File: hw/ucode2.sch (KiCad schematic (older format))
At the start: 16 parts, among them U801 74HC00, U802 74HC590, U803 27C64, U804 27C64, U805 27C64, U806 27C64, U807 74HCT175, U808 74HCT175, U809 74HCT175, U810 74HCT175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

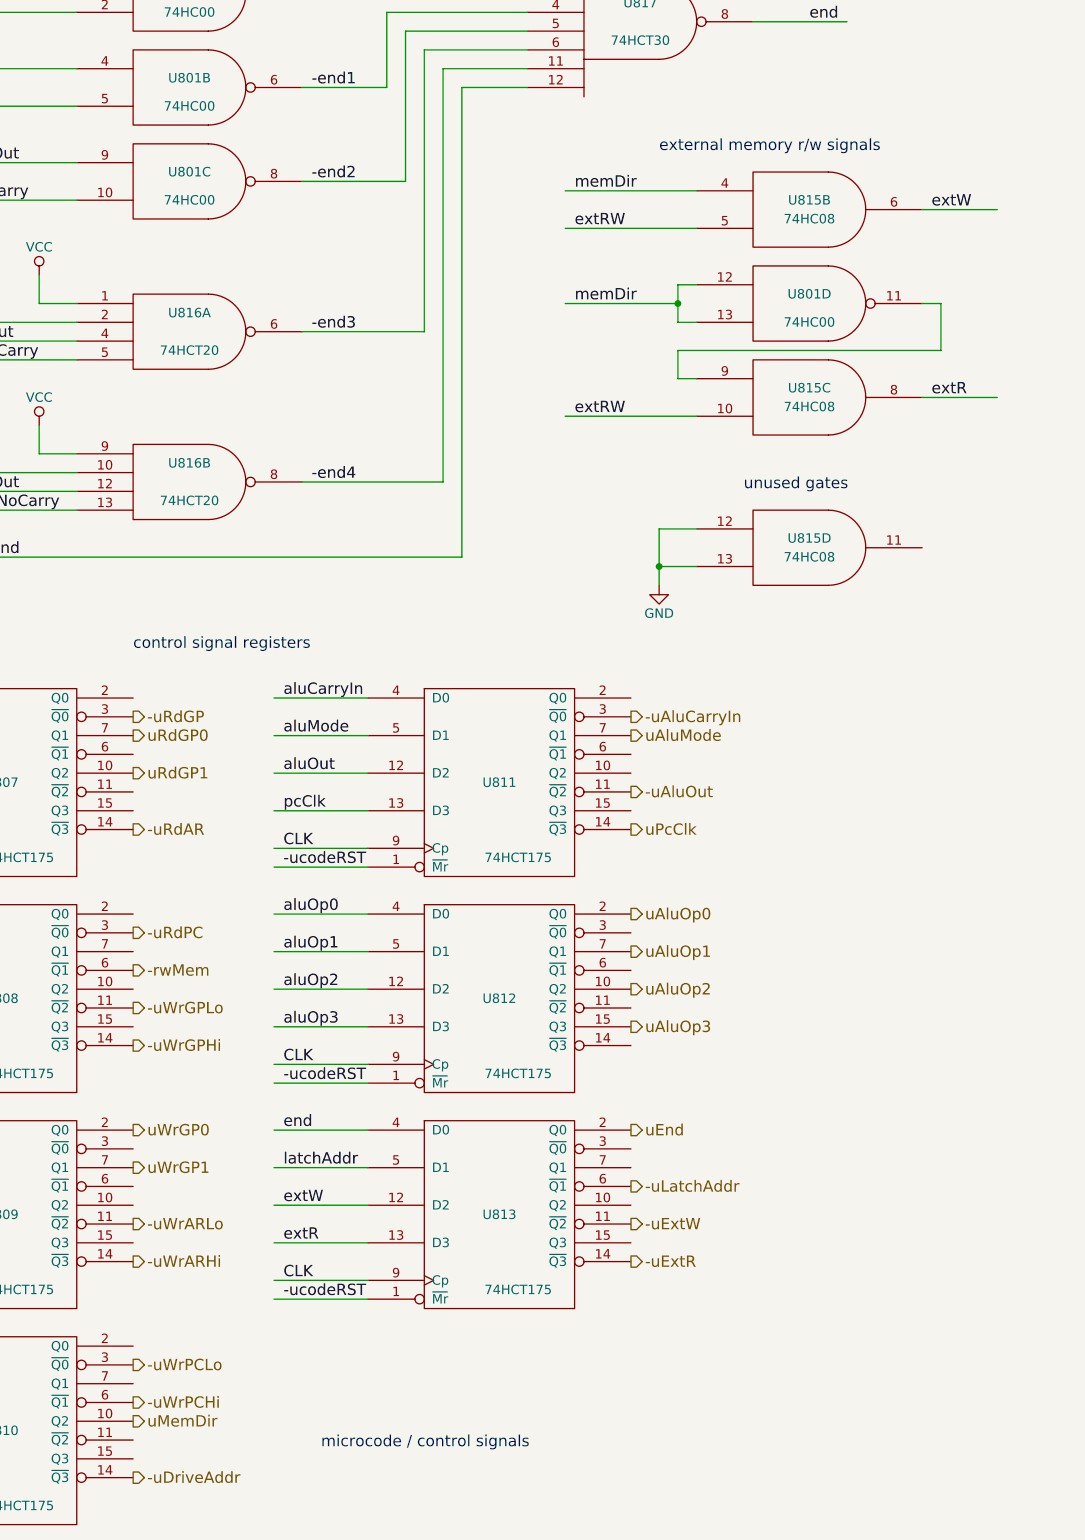
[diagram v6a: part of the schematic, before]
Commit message: do combinational logic for ext r/w after FFs
This should work fine, and allows for one more microcode
signal for latching the ALU condition codes, which I'm
pretty sure we will need.
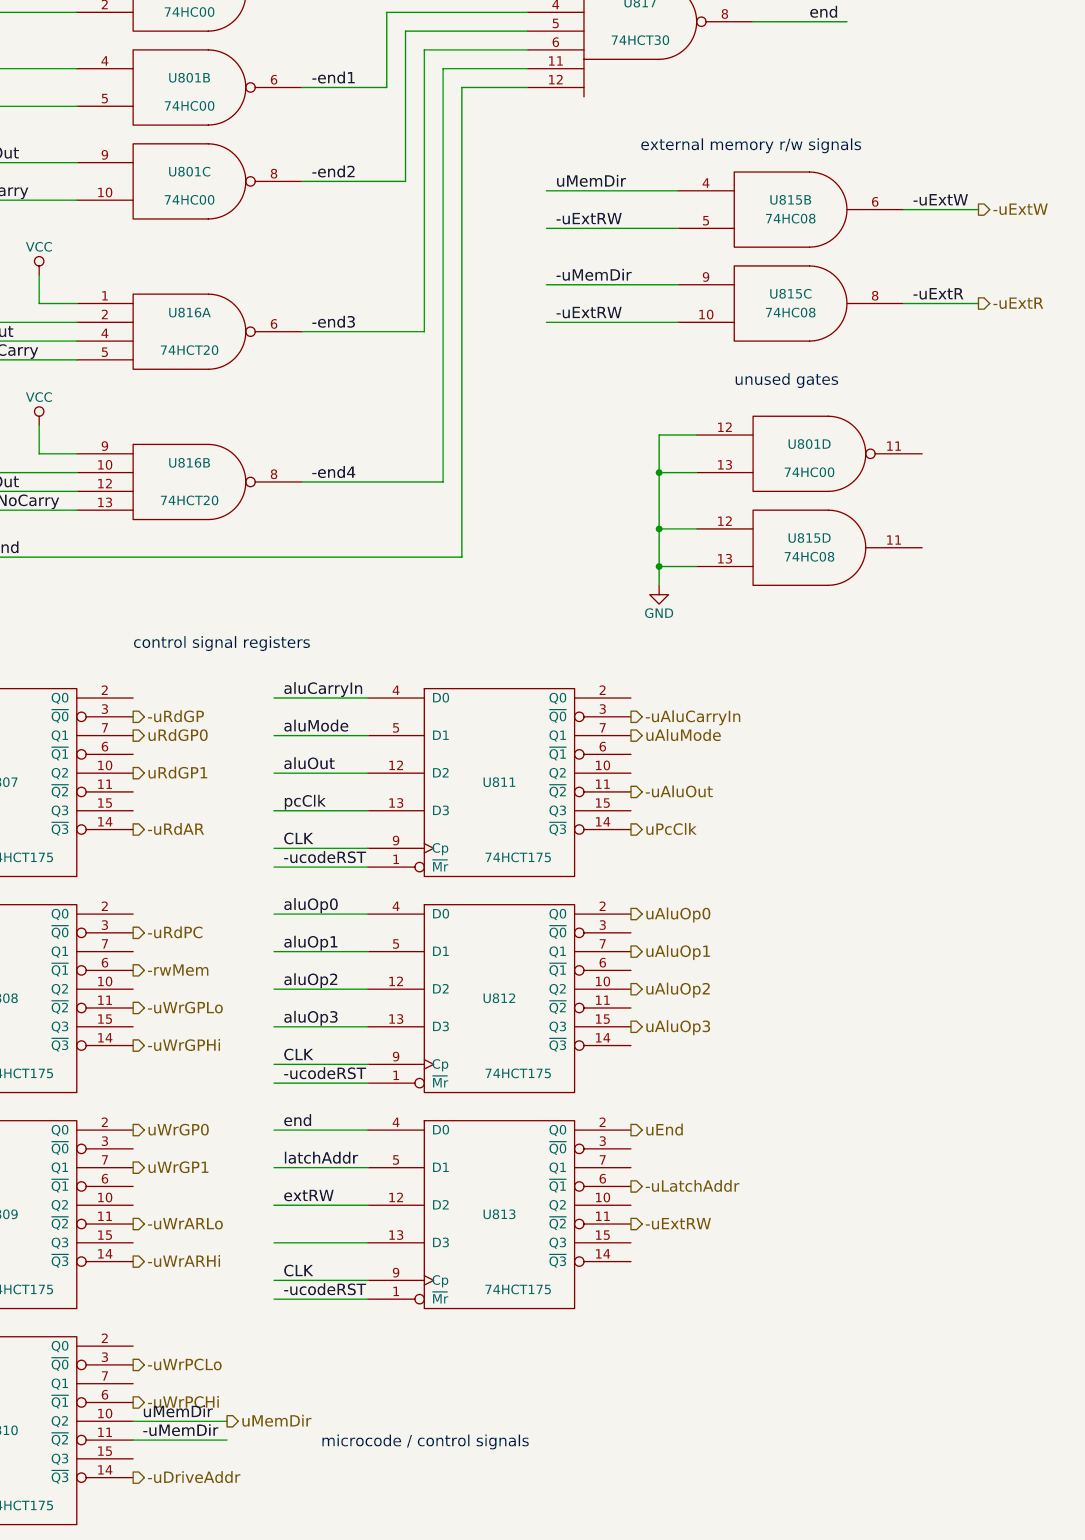
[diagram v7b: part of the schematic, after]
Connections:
- net labels added: -uExtRW, -uMemDir
- net labels removed: extR, extW
- wire segments 247 -> 242
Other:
- moved on the sheet: U815B, U815C
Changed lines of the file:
@@
-	1    0    0    -1
-$EndComp
-$Comp
-L 74LS00 U801
-U 4 1 59522859
-P 11900 3050
-F 0 "U801" H 11900 3100 50  0000 C CNN
-F 1 "74HC00" H 11900 2950 50  0000 C CNN
-F 2 "" H 11900 3050 50  0001 C CNN
-F 3 "" H 11900 3050 50  0001 C CNN
-	4    11900 3050
 	1    0    0    -1
 $EndComp
@@
 Text Label 6450 9000 0    60   ~ 0
 memDir
-Text HLabel 8300 9000 2    60   Output ~ 0
+Text HLabel 8800 9000 2    60   Output ~ 0
 uMemDir
 Text Label 5400 7900 0    60   ~ 0
@@
 	8300 8900 8300 8900
 Wire Wire Line
-	8300 9100 8300 9100
+	8300 9100 8800 9100
 Wire Wire Line
 	8300 9200 8300 9200
@@
 Wire Wire Line
 	6900 9000 6400 9000
-Text Notes 11550 4050 0    60   ~ 0
+Text Notes 11500 3500 0    60   ~ 0
 unused gates
 $Comp
@@
 L 74LS08 U815
 U 2 1 596BBD93
-P 11900 2550
-F 0 "U815" H 11900 2600 50  0000 C CNN
-F 1 "74HC08" H 11900 2500 50  0000 C CNN
-F 2 "" H 11900 2550 50  0001 C CNN
-F 3 "" H 11900 2550 50  0001 C CNN
-	2    11900 2550
-	1    0    0    -1
-$EndComp
-Wire Wire Line
-	11300 2450 10600 2450
-Wire Wire Line
-	11300 2650 10600 2650
-Text Label 10650 2450 0    60   ~ 0
-memDir
-Text Label 10650 2650 0    60   ~ 0
-extRW
-Wire Wire Line
-	12500 2550 12900 2550
-Text Label 12550 2550 0    60   ~ 0
-extW
+P 11800 2550
+F 0 "U815" H 11800 2600 50  0000 C CNN
+F 1 "74HC08" H 11800 2500 50  0000 C CNN
+F 2 "" H 11800 2550 50  0001 C CNN
+F 3 "" H 11800 2550 50  0001 C CNN
+	2    11800 2550
+	1    0    0    -1
+$EndComp
+Wire Wire Line
+	11200 2450 10500 2450
+Wire Wire Line
+	11200 2650 10500 2650
+Text Label 10550 2450 0    60   ~ 0
+uMemDir
+Text Label 10550 2650 0    60   ~ 0
+-uExtRW
+Wire Wire Line
+	12400 2550 12800 2550
+Text Label 12450 2550 0    60   ~ 0
+-uExtW
 $Comp
 L 74LS08 U815
 U 3 1 596BC594
-P 11900 3550
-F 0 "U815" H 11900 3600 50  0000 C CNN
-F 1 "74HC08" H 11900 3500 50  0000 C CNN
-F 2 "" H 11900 3550 50  0001 C CNN
-F 3 "" H 11900 3550 50  0001 C CNN
-	3    11900 3550
-	1    0    0    -1
-$EndComp
-Wire Wire Line
-	11300 3650 10600 3650
-Wire Wire Line
-	10600 3050 11200 3050
-Wire Wire Line
-	11200 2950 11200 3150
-Wire Wire Line
-	11200 2950 11300 2950
-Wire Wire Line
-	11200 3150 11300 3150
-Connection ~ 11200 3050
-Text Label 10650 3050 0    60   ~ 0
-memDir
-Wire Wire Line
-	12500 3050 12600 3050
-Wire Wire Line
-	12600 3050 12600 3300
-Wire Wire Line
-	12600 3300 11200 3300
-Wire Wire Line
-	11200 3300 11200 3450
-Wire Wire Line
-	11200 3450 11300 3450
-Text Label 10650 3650 0    60   ~ 0
-extRW
-Wire Wire Line
-	12500 3550 12900 3550
-Text Label 12550 3550 0    60   ~ 0
-extR
-Text Notes 11100 2250 0    60   ~ 0
+P 11800 3050
+F 0 "U815" H 11800 3100 50  0000 C CNN
+F 1 "74HC08" H 11800 3000 50  0000 C CNN
+F 2 "" H 11800 3050 50  0001 C CNN
+F 3 "" H 11800 3050 50  0001 C CNN
+	3    11800 3050
+	1    0    0    -1
+$EndComp
+Wire Wire Line
+	11200 3150 10500 3150
+Text Label 10550 3150 0    60   ~ 0
+-uExtRW
+Wire Wire Line
+	12400 3050 12800 3050
+Text Label 12450 3050 0    60   ~ 0
+-uExtR
+Text Notes 11000 2250 0    60   ~ 0
 external memory r/w signals
 $Comp
@@
 	11300 4250 11100 4250
 Wire Wire Line
-	11100 4250 11100 4550
+	11100 3750 11100 4550
 Wire Wire Line
 	11300 4450 11100 4450
 Connection ~ 11100 4450
 Text Label 9100 7850 0    60   ~ 0
-extW
-Text Label 9100 8050 0    60   ~ 0
-extR
+extRW
 Text HLabel 10950 7950 2    60   Output ~ 0
+-uExtRW
+Wire Wire Line
+	8300 9000 8800 9000
+Text Label 8350 9000 0    60   ~ 0
+uMemDir
+Text Label 8350 9100 0    60   ~ 0
+-uMemDir
+Wire Wire Line
+	11200 2950 10500 2950
+Text Label 10550 2950 0    60   ~ 0
+-uMemDir
+Text HLabel 12800 2550 2    60   Output ~ 0
 -uExtW
-Text HLabel 10950 8150 2    60   Output ~ 0
+Text HLabel 12800 3050 2    60   Output ~ 0
 -uExtR
+$Comp
+L 74LS00 U801
+U 4 1 596FF174
+P 11900 3850
+F 0 "U801" H 11900 3900 50  0000 C CNN
+F 1 "74HC00" H 11900 3750 50  0000 C CNN
+F 2 "" H 11900 3850 50  0001 C CNN
+F 3 "" H 11900 3850 50  0001 C CNN
+	4    11900 3850
+	1    0    0    -1
+$EndComp
+Wire Wire Line
+	11300 3750 11100 3750
+Connection ~ 11100 4250
+Wire Wire Line
+	11300 3950 11100 3950
+Connection ~ 11100 3950
 $EndSCHEMATC

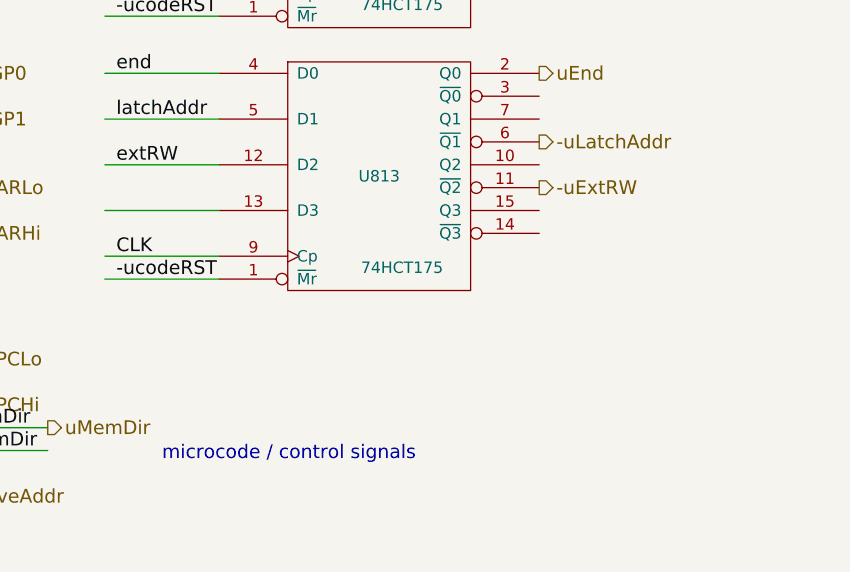
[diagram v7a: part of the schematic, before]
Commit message: add -uExtW/-uExtR signals to main schematic
Also, don't need to export the -uExtRW signal via a
hierarchical pin.
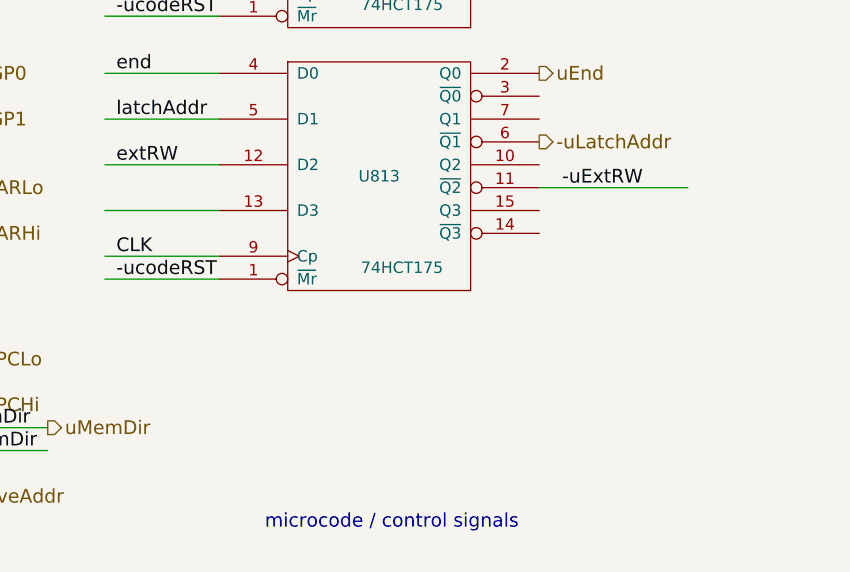
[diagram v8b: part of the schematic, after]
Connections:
- wire segments 242 -> 243
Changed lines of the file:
@@
 EELAYER 25 0
 EELAYER END
-$Descr User 13780 10645
+$Descr User 14173 10953
 encoding utf-8
 Sheet 9 10
@@
 Text HLabel 8300 5850 2    60   Output ~ 0
 -uRdAR
-Text Notes 9300 9150 0    60   ~ 0
+Text Notes 9750 9450 0    60   ~ 0
 microcode / control signals
 Text HLabel 8300 6400 2    60   Output ~ 0
@@
 Text Label 9100 7850 0    60   ~ 0
 extRW
-Text HLabel 10950 7950 2    60   Output ~ 0
--uExtRW
 Wire Wire Line
 	8300 9000 8800 9000
@@
 	11300 3950 11100 3950
 Connection ~ 11100 3950
+Wire Wire Line
+	10950 7950 11600 7950
+Text Label 11050 7950 0    60   ~ 0
+-uExtRW
 $EndSCHEMATC
